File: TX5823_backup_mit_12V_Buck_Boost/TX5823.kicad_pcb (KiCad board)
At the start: 2 copper layers, 72 parts, among them IC1 ATMEGA328P-A, IC2 ATTINY13A-SS, P1 Akku_in, P2 ISP, P3 Mavlink, Q3 MOSFET_N, SW1 SW_PUSH, SW2 SW_PUSH, U2 TPS54531, U3 TPS7A7200RGT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

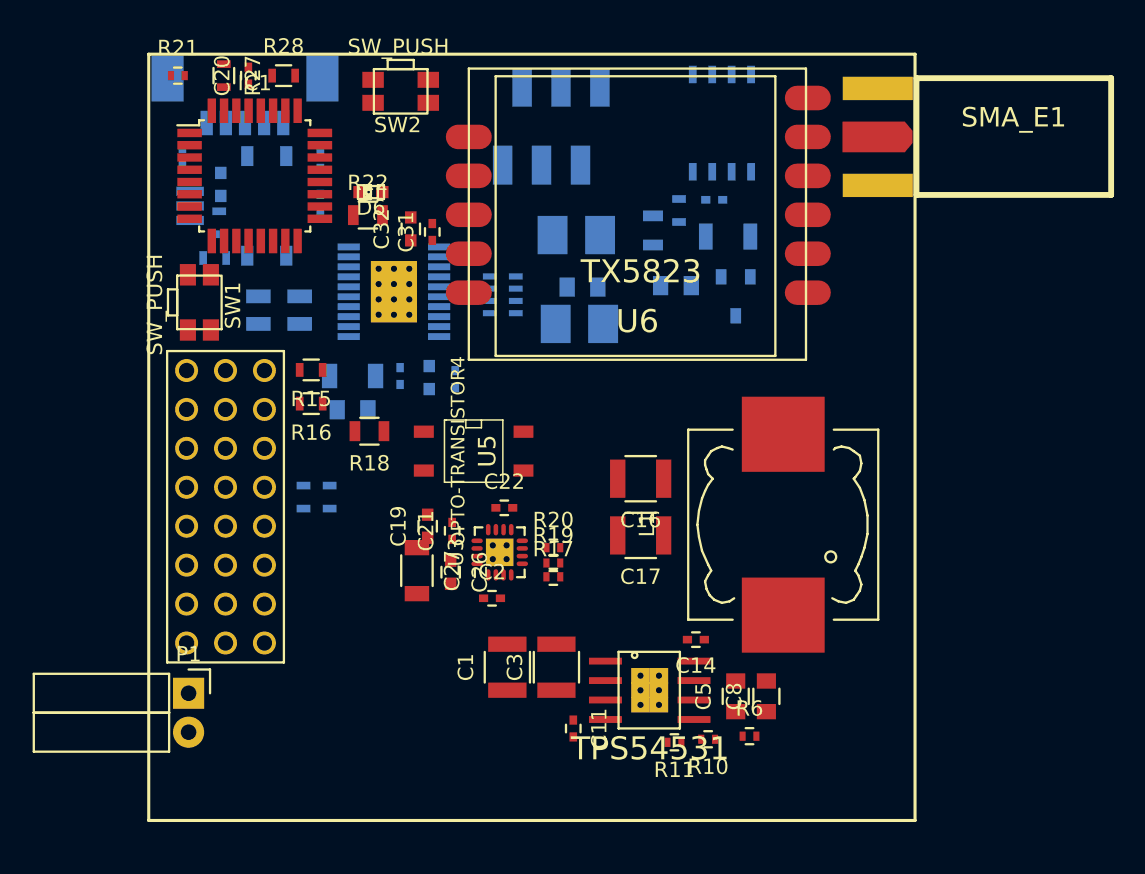
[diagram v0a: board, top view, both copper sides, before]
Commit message: 12V Wandler entfernt
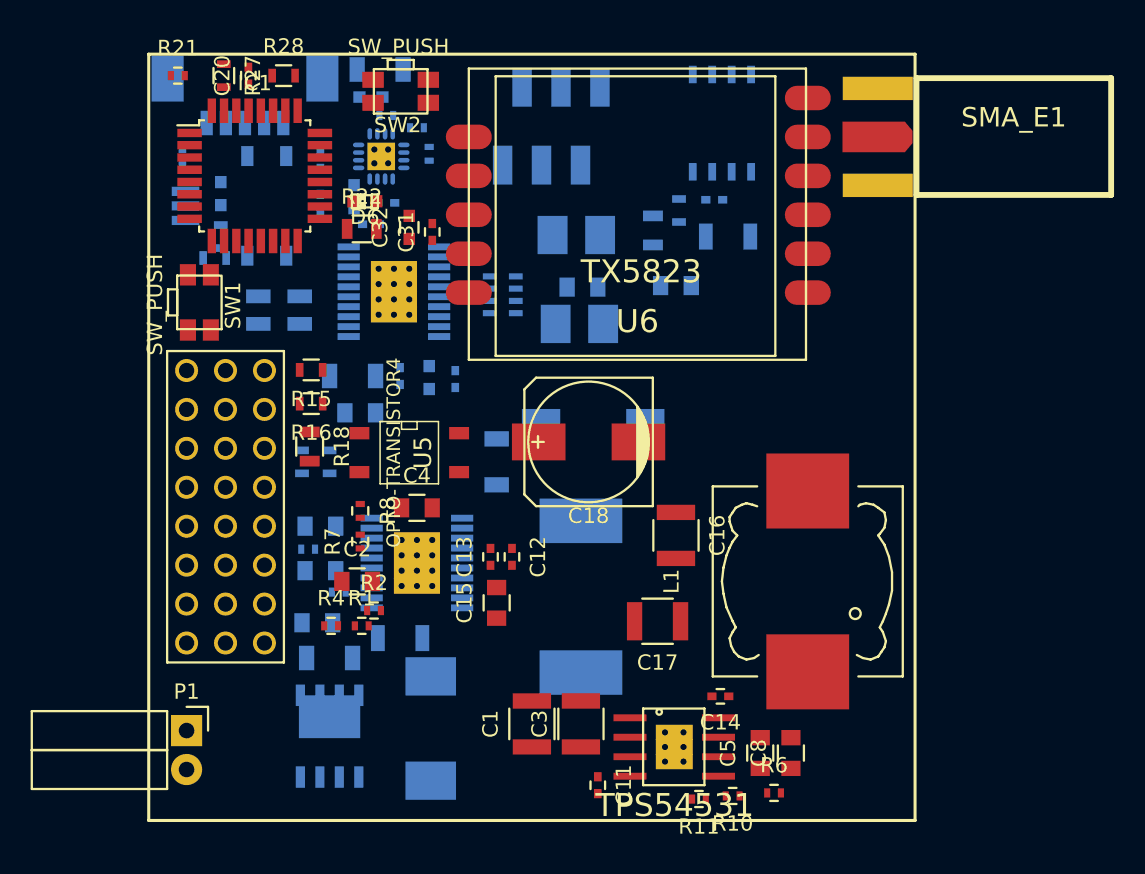
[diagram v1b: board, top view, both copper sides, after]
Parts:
- removed Q3: MOSFET_N, toni:SOT23_GDS
- added C10: Ccomp, Capacitors_SMD:C_0805, B.Cu at (86.2, 50.8)
- added C12: Cvccx, Capacitors_SMD:C_0402, F.Cu at (98.7, 52.8)
- added C13: Cvcc, Capacitors_SMD:C_0402, F.Cu at (97.3, 52.8)
- added C15: Cboot, Capacitors_SMD:C_0805, F.Cu at (97.7, 55.8)
- added C18: Cout, Capacitors_SMD:c_elec_8x10, F.Cu at (103.7, 45.3)
- added C38: 1uF/50V, Capacitors_SMD:C_1206, B.Cu at (97.7, 46.6)
- added C4: Css, Capacitors_SMD:C_0805, F.Cu at (92.5, 49.6)
- added C6: Cin, Capacitors_SMD:C_1206, B.Cu at (86.8, 59.4)
- added C7: Ccomp2, Capacitors_SMD:C_0805, B.Cu at (86.2, 53.7)
- added C9: Cinx, Capacitors_SMD:C_0805, B.Cu at (86.0, 57.1)
- added D2: DIODESCH, Diodes_SMD:Diode-SMC_Standard, B.Cu at (93.4, 64.0)
- added D5: DIODESCH, Diodes_SMD:Diode-SMC_Standard, B.Cu at (104.0, 44.8)
- added L2: 15uH, Choke_SMD:Choke_SMD_12x12mm_h4.5mm, B.Cu at (103.2, 55.4)
- added Q1: MOS_N, toni:SO8_WITH_EP, B.Cu at (86.8, 64.5)
- added R1: Ruv1, Resistors_SMD:R_0402, F.Cu at (88.9, 57.3)
- added R2: Ruv2, Resistors_SMD:R_0402, F.Cu at (89.7, 56.3)
- added R3: Rt, Resistors_SMD:R_0402, B.Cu at (87.4, 55.1)
- added R4: Renable, Resistors_SMD:R_0402, F.Cu at (86.9, 57.3)
- added R5: Rcomp, Resistors_SMD:R_0402, B.Cu at (85.4, 52.3)
- added R7: Rfbb, Resistors_SMD:R_0402, F.Cu at (88.8, 51.8)
- added R8: Rfbt, Resistors_SMD:R_0402, F.Cu at (88.8, 49.8)
- added R9: Rsense, Resistors_SMD:R_1206, B.Cu at (91.4, 58.1)
- added U1: LM25118, toni:TSSOP-20_4.4x6.5mm_Pitch0.65mm_EP, B.Cu at (92.5, 53.2)
- C19, C21, C22, C26, C27, R17, R19, R20, U3: moved to B.Cu
- C2: value 220pF -> Cramp; footprint Capacitors_SMD:C_0402 -> Capacitors_SMD:C_0805
- moved C27 32.8 mm to (90.1, 21.0), turned to 0 degrees
- moved R17 32.0 mm to (90.5, 24.0), turned to 180 degrees
- moved C26 31.4 mm to (89.5, 22.8), turned to 0 degrees
- moved R19 29.8 mm to (92.5, 24.8)
- moved U3 27.0 mm to (90.2, 26.7), turned to 270 degrees
- moved R20 26.9 mm to (93.3, 26.5), turned to 270 degrees
- moved C19 22.0 mm to (88.4, 29.3), turned to 270 degrees
- moved C22 21.3 mm to (90.5, 29.7)
- moved C21 20.7 mm to (89.5, 31.1), turned to 0 degrees
- moved C2 8.87 mm to (88.6, 54.4)
- moved C17 5.71 mm to (108.2, 57.0)
- moved C16 4.36 mm to (109.4, 51.4), turned to 270 degrees
- moved U5 4.20 mm to (92.0, 46.0)
- moved C3 4.03 mm to (103.2, 63.7)
- moved C1 4.03 mm to (100.0, 63.7)
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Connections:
- C2 pad 1: +3.3V -> Net-(C2-Pad1)
- C2 pad 2: Net-(C2-Pad2) -> GND
- C26 pad 2: GND -> Net-(C26-Pad2)
- C27 pad 2: GND -> Net-(C26-Pad2)
- U3 pad 2: Net-(C2-Pad2) -> Net-(C26-Pad2)
